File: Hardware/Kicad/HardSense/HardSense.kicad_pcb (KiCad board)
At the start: 2 copper layers, 45.7 x 50.8 mm, 12 parts, among them J1 Conn_01x02, U1 ESP32-DEVKITC-32D

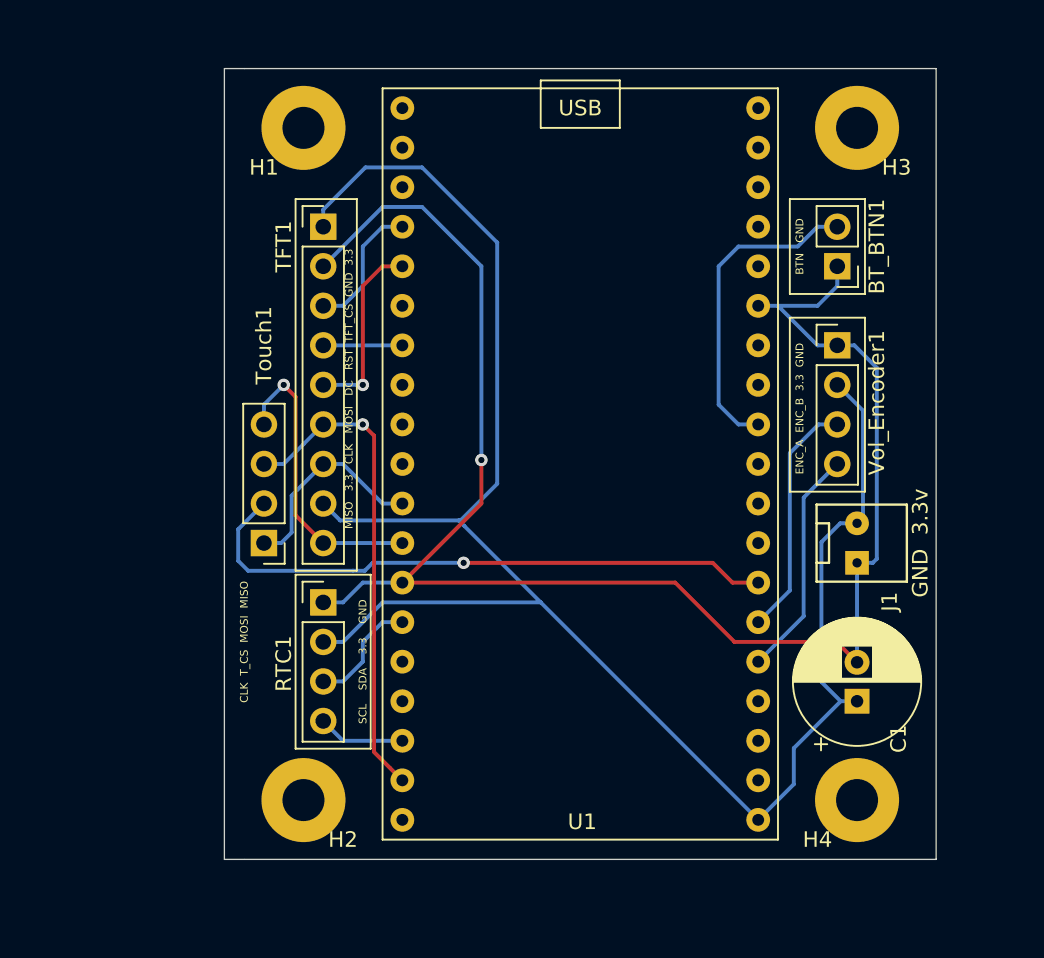
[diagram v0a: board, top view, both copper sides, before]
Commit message: New PCB board for HardSense
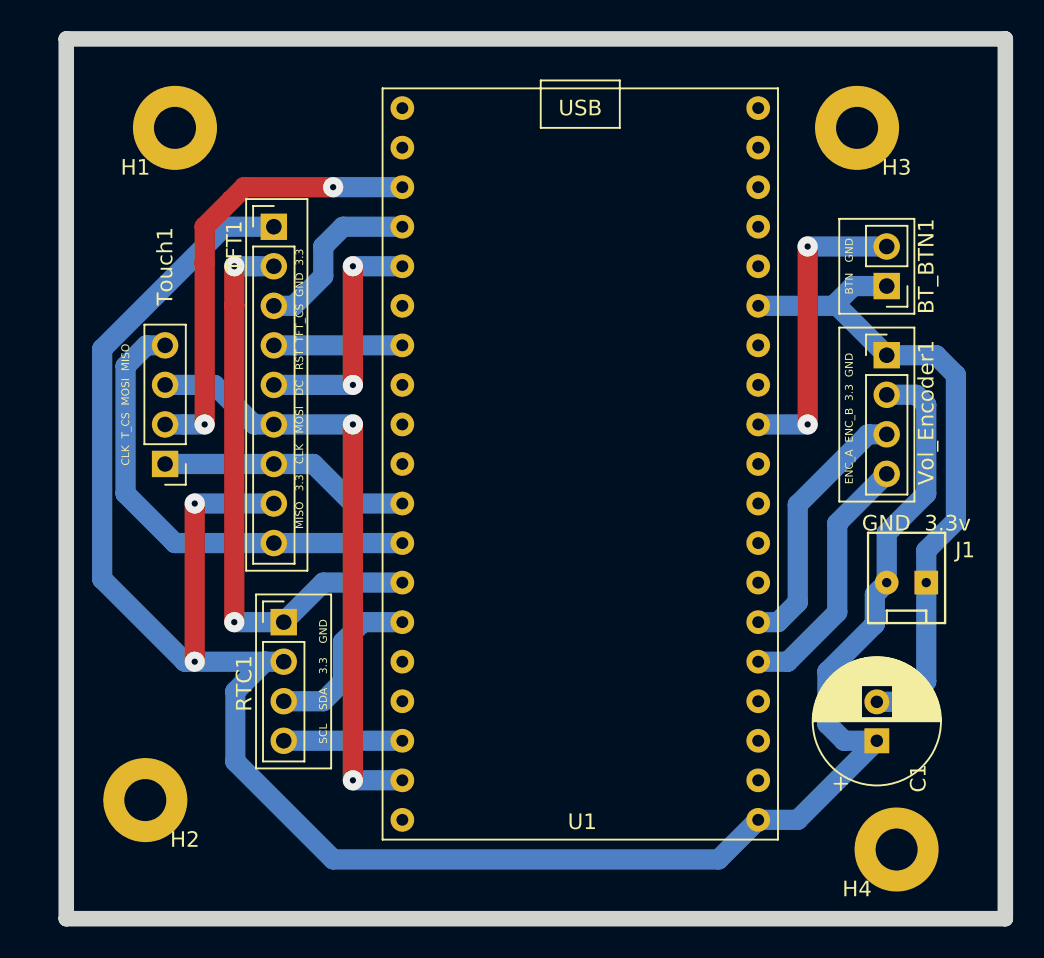
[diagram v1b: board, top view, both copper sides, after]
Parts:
- moved H2 10.2 mm to (113.0, 102.9)
- moved H1 8.25 mm to (114.9, 59.7)
- moved Touch1 8.13 mm to (114.3, 81.3)
- moved J1 4.26 mm to (160.7, 88.9), turned to 270 degrees
- moved H4 4.07 mm to (161.3, 106.0)
- moved BT_BTN1 3.42 mm to (160.7, 69.8)
- moved Vol_Encoder1 3.24 mm to (160.7, 74.3)
- moved TFT1 3.17 mm to (121.3, 66.0)
- moved C1 2.84 mm to (160.0, 99.1)
- moved RTC1 2.84 mm to (121.9, 91.4)
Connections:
- BT_BTN1 pad 1: GND -> GNDA
- C1 pad 2: GND -> GNDA
- J1 pad 1: GND -> GNDA
- U1 pad 14: GND -> GNDA
- U1 pad 36: Net-(U1-Pad36) -> /T_CS
- U1 pad 7: /T_CS -> Net-(U1-Pad7)
- Vol_Encoder1 pad 1: GND -> GNDA
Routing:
- net GND: track 107.6 -> 37.2 mm, vias 1 -> 2
- net GNDA: track 0.00 -> 42.7 mm
- net 3.3V: track 119.9 -> 141.9 mm, vias 0 -> 2
- net /SPI_MISO: track 19.4 -> 30.4 mm, vias 1 -> 0
- net /T_CS: track 38.8 -> 29.0 mm, vias 1 -> 2
- net /SPI_MOSI: track 31.3 -> 39.2 mm, vias 1 -> 2
- net /TFT_DC: track 12.0 -> 15.9 mm, vias 1 -> 2
- net /SDA: track 7.76 -> 11.6 mm
- net /TFT_RST: track 5.08 -> 8.25 mm
- net /SPI_CLK: track 13.4 -> 16.3 mm
- net /TFT_CS: track 8.67 -> 11.5 mm
- net /SCL: track 5.61 -> 7.62 mm
- net /ENC_A: track 14.8 -> 16.6 mm
- net /ENC_B: track 15.5 -> 16.9 mm
- net /BT_BTN: track 20.6 -> 19.7 mm, vias 0 -> 2
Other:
- board size 45.7 x 50.8 mm -> 60.3 x 56.5 mm
- net class Default: trace_width 0.25 -> 1.3; via_dia 0.8 -> 1.3

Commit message: Small change to PCB.  Rotated the button header and moved a couple traces.
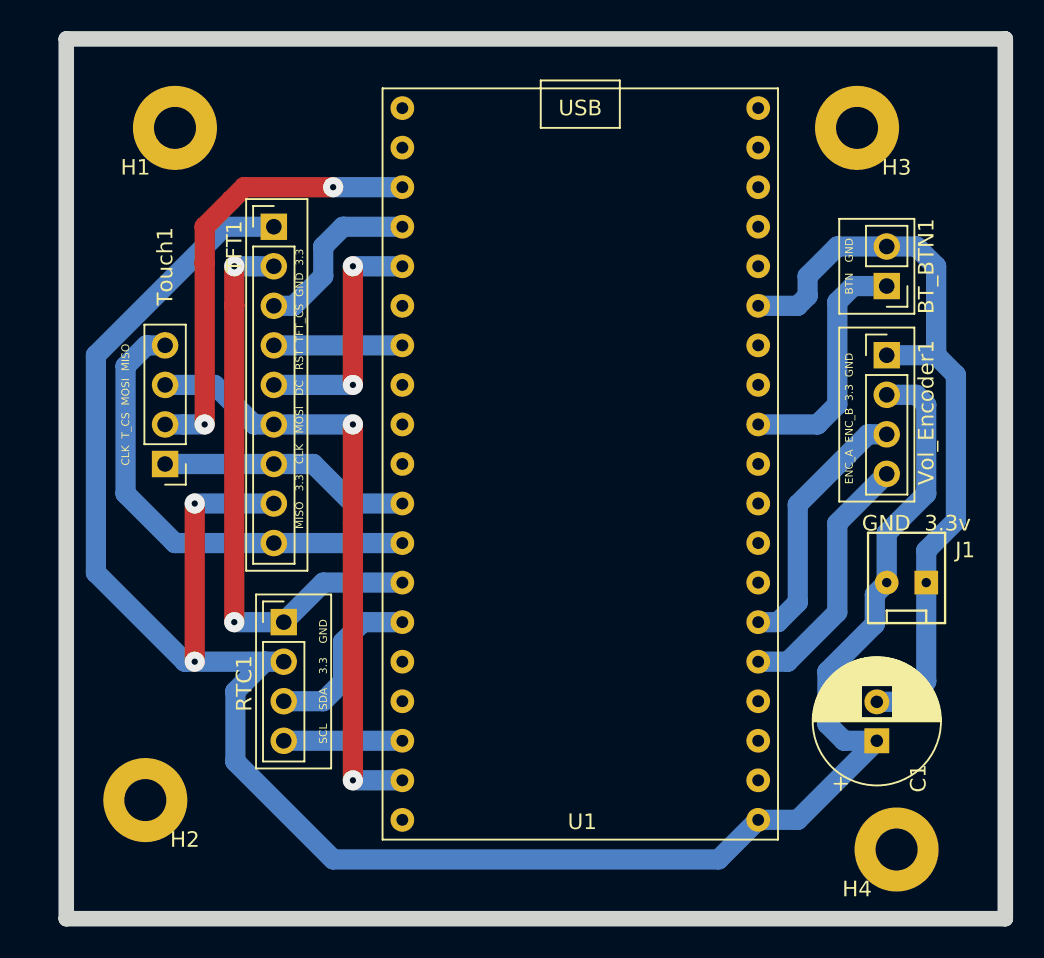
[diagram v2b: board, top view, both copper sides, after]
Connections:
- BT_BTN1 pad 1: GNDA -> /BT_BTN
- BT_BTN1 pad 2: /BT_BTN -> GNDA
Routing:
- net GNDA: track 42.7 -> 49.2 mm
- net /BT_BTN: track 19.7 -> 15.8 mm, vias 2 -> 0
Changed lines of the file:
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@@
     (thickness 1.6)
     (drawings 33)
-    (tracks 111)
+    (tracks 114)
     (zones 0)
     (modules 12)
@@
     (fp_line (start -0.635 -1.27) (end 1.27 -1.27) (layer F.Fab) (width 0.1))
     (pad 2 thru_hole oval (at 0 2.54 180) (size 1.7 1.7) (drill 1) (layers *.Cu *.Mask)
+      (net 38 GNDA))
+    (pad 1 thru_hole rect (at 0 0 180) (size 1.7 1.7) (drill 1) (layers *.Cu *.Mask)
       (net 12 /BT_BTN))
-    (pad 1 thru_hole rect (at 0 0 180) (size 1.7 1.7) (drill 1) (layers *.Cu *.Mask)
-      (net 38 GNDA))
     (model ${KISYS3DMOD}/Connector_PinHeader_2.54mm.3dshapes/PinHeader_1x02_P2.54mm_Vertical.wrl
       (at (xyz 0 0 0))
@@
     (effects (font (size 1 1) (thickness 0.15)))
   )
-  (segment (start 158.505 69.85) (end 157.235 71.12) (width 1.3) (layer B.Cu) (net 38))
-  (segment (start 160.655 69.85) (end 158.505 69.85) (width 1.3) (layer B.Cu) (net 38))
-  (segment (start 157.235 71.12) (end 152.4 71.12) (width 1.3) (layer B.Cu) (net 38))
-  (segment (start 157.48 71.12) (end 157.235 71.12) (width 1.3) (layer B.Cu) (net 38))
-  (segment (start 160.655 74.295) (end 157.48 71.12) (width 1.3) (layer B.Cu) (net 38))
-  (segment (start 161.885 96.56) (end 160.02 96.56) (width 1.3) (layer B.Cu) (net 38))
-  (segment (start 163.195 88.9) (end 163.195 95.25) (width 1.3) (layer B.Cu) (net 38))
-  (segment (start 163.195 95.25) (end 161.885 96.56) (width 1.3) (layer B.Cu) (net 38))
-  (segment (start 163.195 86.838) (end 165.1 84.933) (width 1.3) (layer B.Cu) (net 38))
-  (segment (start 163.195 88.9) (end 163.195 86.838) (width 1.3) (layer B.Cu) (net 38))
-  (segment (start 165.1 84.933) (end 165.1 75.565) (width 1.3) (layer B.Cu) (net 38))
-  (segment (start 163.83 74.295) (end 160.655 74.295) (width 1.3) (layer B.Cu) (net 38))
-  (segment (start 165.1 75.565) (end 163.83 74.295) (width 1.3) (layer B.Cu) (net 38))
   (segment (start 124.46 88.9) (end 129.54 88.9) (width 1.3) (layer B.Cu) (net 1))
   (segment (start 121.92 91.44) (end 124.46 88.9) (width 1.3) (layer B.Cu) (net 1))
@@
   (segment (start 149.86 106.68) (end 152.4 104.14) (width 1.3) (layer B.Cu) (net 2))
   (segment (start 125.095 106.68) (end 149.86 106.68) (width 1.3) (layer B.Cu) (net 2))
-  (segment (start 115.57 93.98) (end 120.717919 93.98) (width 1.3) (layer B.Cu) (net 2))
-  (segment (start 110.25999 88.66999) (end 115.57 93.98) (width 1.3) (layer B.Cu) (net 2))
-  (segment (start 110.25999 73.89001) (end 110.25999 88.66999) (width 1.3) (layer B.Cu) (net 2))
-  (segment (start 121.285 66.04) (end 118.11 66.04) (width 1.3) (layer B.Cu) (net 2))
-  (segment (start 118.11 66.04) (end 110.25999 73.89001) (width 1.3) (layer B.Cu) (net 2))
   (segment (start 121.285 83.82) (end 116.205 83.82) (width 1.3) (layer B.Cu) (net 2))
   (via (at 116.205 83.82) (size 1.3) (drill 0.4) (layers F.Cu B.Cu) (net 2))
   (segment (start 116.205 83.82) (end 116.205 93.98) (width 1.3) (layer F.Cu) (net 2))
   (via (at 116.205 93.98) (size 1.3) (drill 0.4) (layers F.Cu B.Cu) (net 2))
+  (segment (start 115.57 93.98) (end 120.717919 93.98) (width 1.3) (layer B.Cu) (net 2))
+  (segment (start 109.855 88.265) (end 115.57 93.98) (width 1.3) (layer B.Cu) (net 2))
+  (segment (start 109.855 74.295) (end 109.855 88.265) (width 1.3) (layer B.Cu) (net 2))
+  (segment (start 121.285 66.04) (end 118.11 66.04) (width 1.3) (layer B.Cu) (net 2))
+  (segment (start 118.11 66.04) (end 109.855 74.295) (width 1.3) (layer B.Cu) (net 2))
   (segment (start 121.285 86.36) (end 129.54 86.36) (width 1.3) (layer B.Cu) (net 3))
   (segment (start 113.097919 73.66) (end 111.76 74.997919) (width 1.3) (layer B.Cu) (net 3))
@@
   (segment (start 154.94 90.17) (end 153.67 91.44) (width 1.3) (layer B.Cu) (net 11))
   (segment (start 153.67 91.44) (end 152.4 91.44) (width 1.3) (layer B.Cu) (net 11))
-  (segment (start 160.655 67.31) (end 155.575 67.31) (width 1.3) (layer B.Cu) (net 12))
-  (via (at 155.575 67.31) (size 1.3) (drill 0.4) (layers F.Cu B.Cu) (net 12))
-  (segment (start 155.575 67.31) (end 155.575 78.74) (width 1.3) (layer F.Cu) (net 12))
-  (via (at 155.575 78.74) (size 1.3) (drill 0.4) (layers F.Cu B.Cu) (net 12))
-  (segment (start 155.575 78.74) (end 152.4 78.74) (width 1.3) (layer B.Cu) (net 12))
+  (segment (start 158.505 69.85) (end 157.48 70.875) (width 1.3) (layer B.Cu) (net 12))
+  (segment (start 160.655 69.85) (end 158.505 69.85) (width 1.3) (layer B.Cu) (net 12))
+  (segment (start 157.48 70.875) (end 157.48 77.47) (width 1.3) (layer B.Cu) (net 12))
+  (segment (start 157.48 77.47) (end 156.21 78.74) (width 1.3) (layer B.Cu) (net 12))
+  (segment (start 156.21 78.74) (end 152.4 78.74) (width 1.3) (layer B.Cu) (net 12))
   (segment (start 121.92 99.06) (end 129.54 99.06) (width 1.3) (layer B.Cu) (net 13))
   (segment (start 129.286 91.694) (end 129.54 91.44) (width 0.25) (layer B.Cu) (net 14))
@@
   (segment (start 125.73 92.71) (end 127 91.44) (width 1.3) (layer B.Cu) (net 14))
   (segment (start 127 91.44) (end 129.54 91.44) (width 1.3) (layer B.Cu) (net 14))
+  (segment (start 161.885 96.56) (end 160.02 96.56) (width 1.3) (layer B.Cu) (net 38))
+  (segment (start 163.195 88.9) (end 163.195 95.25) (width 1.3) (layer B.Cu) (net 38))
+  (segment (start 163.195 95.25) (end 161.885 96.56) (width 1.3) (layer B.Cu) (net 38))
+  (segment (start 163.195 86.838) (end 165.1 84.933) (width 1.3) (layer B.Cu) (net 38))
+  (segment (start 163.195 88.9) (end 163.195 86.838) (width 1.3) (layer B.Cu) (net 38))
+  (segment (start 165.1 84.933) (end 165.1 75.565) (width 1.3) (layer B.Cu) (net 38))
+  (segment (start 163.83 74.295) (end 160.655 74.295) (width 1.3) (layer B.Cu) (net 38))
+  (segment (start 165.1 75.565) (end 163.83 74.295) (width 1.3) (layer B.Cu) (net 38))
+  (segment (start 160.655 67.31) (end 162.56 67.31) (width 1.3) (layer B.Cu) (net 38))
+  (segment (start 163.83 68.58) (end 163.83 74.295) (width 1.3) (layer B.Cu) (net 38))
+  (segment (start 162.56 67.31) (end 163.83 68.58) (width 1.3) (layer B.Cu) (net 38))
+  (segment (start 160.655 67.31) (end 157.48 67.31) (width 1.3) (layer B.Cu) (net 38))
+  (segment (start 157.48 67.31) (end 155.575 69.215) (width 1.3) (layer B.Cu) (net 38))
+  (segment (start 155.575 69.215) (end 155.575 70.485) (width 1.3) (layer B.Cu) (net 38))
+  (segment (start 155.575 70.485) (end 154.94 71.12) (width 1.3) (layer B.Cu) (net 38))
+  (segment (start 154.94 71.12) (end 152.4 71.12) (width 1.3) (layer B.Cu) (net 38))
 )
